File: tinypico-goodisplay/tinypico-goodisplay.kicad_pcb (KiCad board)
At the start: 2 copper layers, 42.5 x 17.8 mm, 24 parts, among them J1 AFC24-S24FIC-00, Q1 Si1308, U1 TinypicoESP32_Symbol

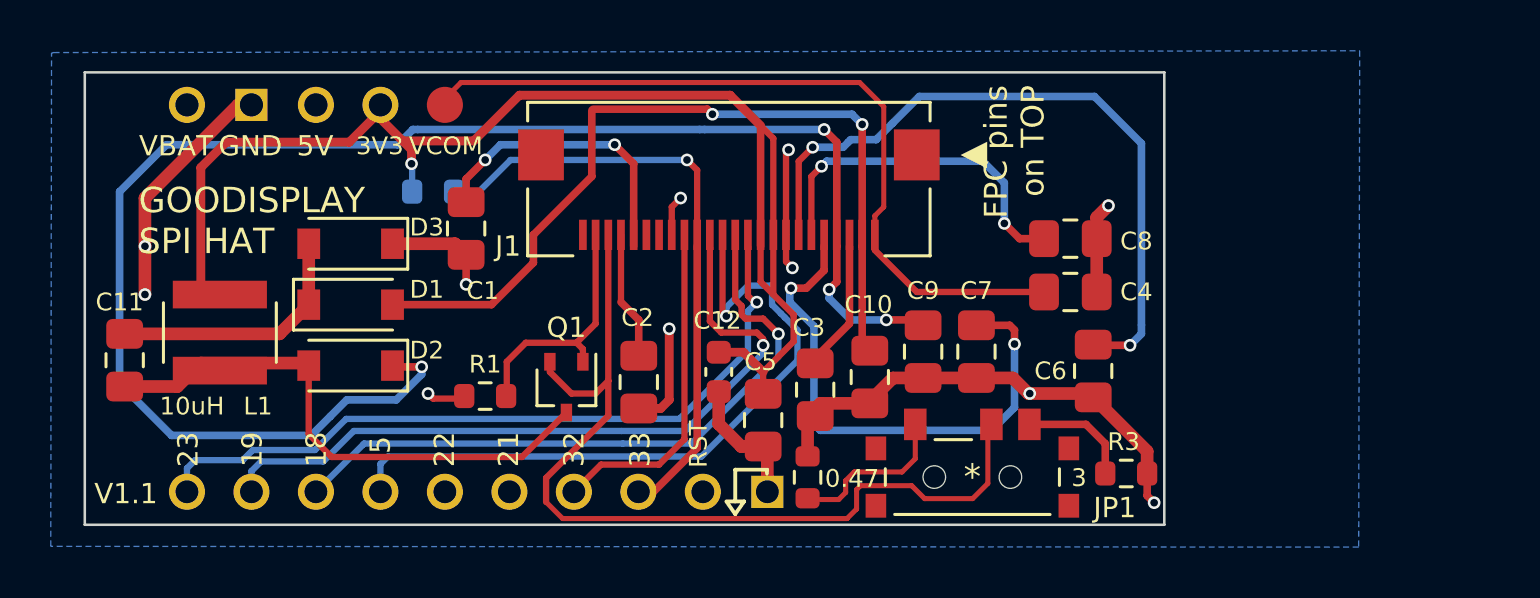
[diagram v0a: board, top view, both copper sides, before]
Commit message: #2 Add PCF8563 RTC
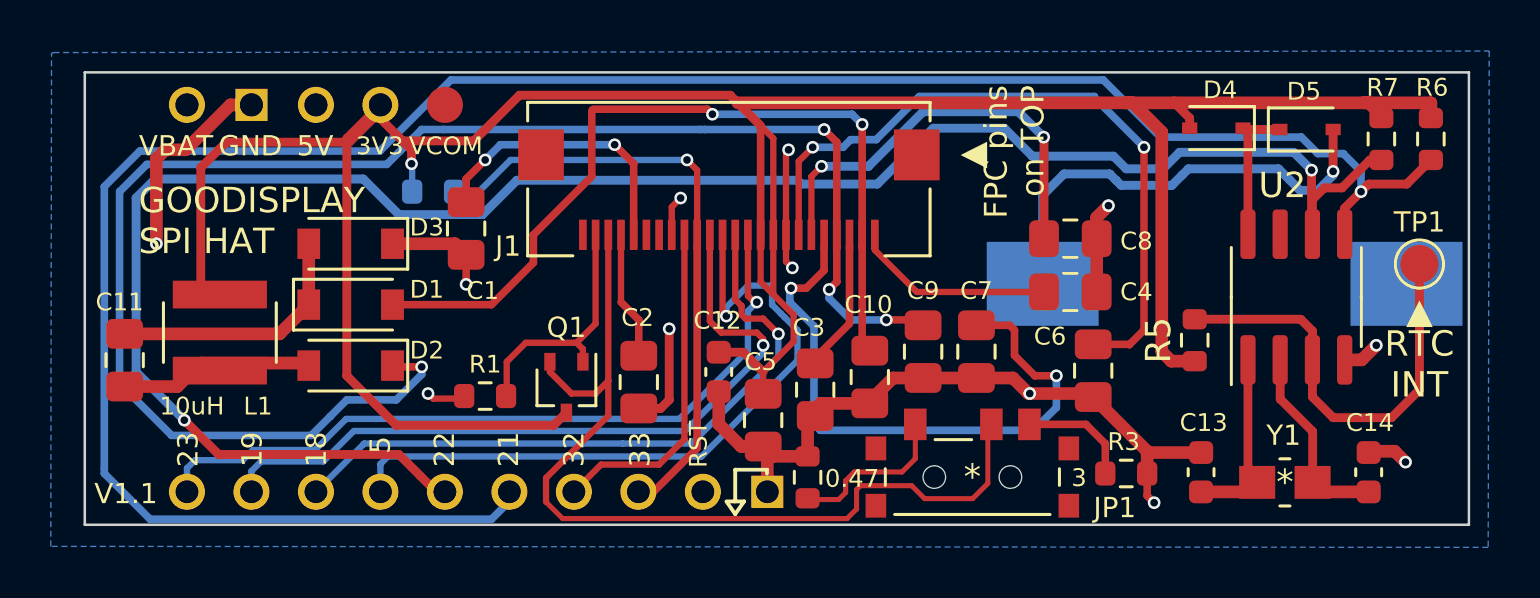
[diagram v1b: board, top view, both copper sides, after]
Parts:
- added BT1: LR44, footprint:C964716_LR44, B.Cu at (117.1, 43.0)
- added C13: 12 pF, Capacitor_SMD:C_0603_1608Metric, F.Cu at (116.2, 50.5)
- added C14: 12 pF, Capacitor_SMD:C_0603_1608Metric, F.Cu at (122.8, 50.5)
- added D4: 1N4148WS, Diode_SMD:D_SOD-323, F.Cu at (116.8, 37.0)
- added D5: 1N4148WS, Diode_SMD:D_SOD-323, F.Cu at (120.3, 37.0)
- added R5: 10 K, Resistor_SMD:R_0603_1608Metric, F.Cu at (116.0, 45.4)
- added R6: 4.7K, Resistor_SMD:R_0603_1608Metric, F.Cu at (125.2, 37.4)
- added R7: 4.7K, Resistor_SMD:R_0603_1608Metric, F.Cu at (123.3, 37.4)
- added TP1: RTC_INT, TestPoint:TestPoint_Pad_D1.5mm, F.Cu at (124.8, 42.4)
- added U2: PCF8563T, Package_SO:SOIC-8_3.9x4.9mm_P1.27mm, F.Cu at (120.0, 43.6)
- added Y1: Crystal_Small, footprint:Q13FC1350000400-Crystal, F.Cu at (119.5, 51.0)
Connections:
- Q1 pad 3: Net-(C11-Pad2) -> +3V3
- U1 pad 15: unconnected-(U1-Pad15) -> /I2C_SDA
- U1 pad 16: unconnected-(U1-Pad16) -> /I2C_SCL
- U1 pad 5: /VCOM -> unconnected-(U1-Pad5)
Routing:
- net /I2C_SDA: track 0.00 -> 87.4 mm, vias 0 -> 1
- net /I2C_SCL: track 0.00 -> 78.2 mm, vias 0 -> 2
- net +3V3: track 52.4 -> 115.3 mm
- net /VCOM: track 31.3 -> 7.95 mm
- net Net-(BT1-Pad1): track 0.00 -> 18.1 mm, vias 0 -> 1
- net Net-(R5-Pad2): track 0.00 -> 17.4 mm
- net Net-(C11-Pad2): track 21.6 -> 7.67 mm
- net Net-(C14-Pad2): track 0.00 -> 7.72 mm
- net Net-(C13-Pad2): track 0.00 -> 7.34 mm
- net Net-(D4-Pad1): track 0.00 -> 5.73 mm
- net GND: track 53.0 -> 58.7 mm, vias 11 -> 12
- net Net-(C8-Pad2): track 13.9 -> 16.9 mm
- net Net-(C7-Pad2): track 21.3 -> 24.1 mm
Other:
- board size 42.5 x 17.8 mm -> 54.5 x 17.8 mm
- board text added: "RTC INT"
- board text added: "▲"
- board text removed: "Designed by:"

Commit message: Correct routing, remove RTC TP1
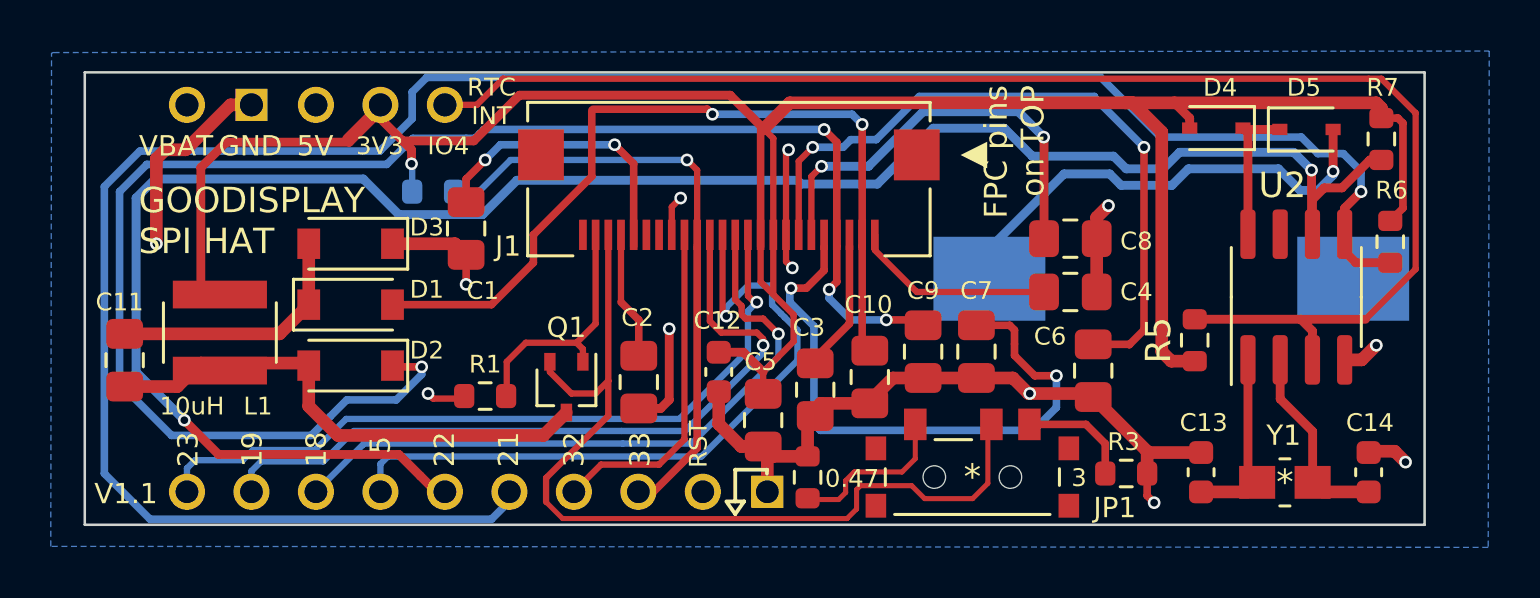
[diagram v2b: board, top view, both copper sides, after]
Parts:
- removed TP1: RTC_INT, TestPoint:TestPoint_Pad_D1.5mm
- moved R6 4.35 mm to (123.7, 41.5)
- moved BT1 2.11 mm to (115.0, 42.9)
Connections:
- Q1 pad 3: +3V3 -> Net-(C11-Pad2)
- R5 pad 2: Net-(R5-Pad2) -> /RTC_INT
- U1 pad 5: unconnected-(U1-Pad5) -> /RTC_INT
- U2 pad 3: Net-(R5-Pad2) -> /RTC_INT
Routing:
- net /RTC_INT: track 0.00 -> 56.7 mm
- net +3V3: track 115.3 -> 97.8 mm
- net Net-(R5-Pad2): track 17.4 -> 0.00 mm
- net Net-(C11-Pad2): track 7.67 -> 20.3 mm
- net Net-(BT1-Pad1): track 18.1 -> 18.8 mm
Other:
- board size 54.5 x 17.8 mm -> 52.8 x 17.8 mm
- board text added: "IO4"
- board text removed: "VCOM"
- board text removed: "▲"

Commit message: #2 Add CR1220 as optional RTC backup
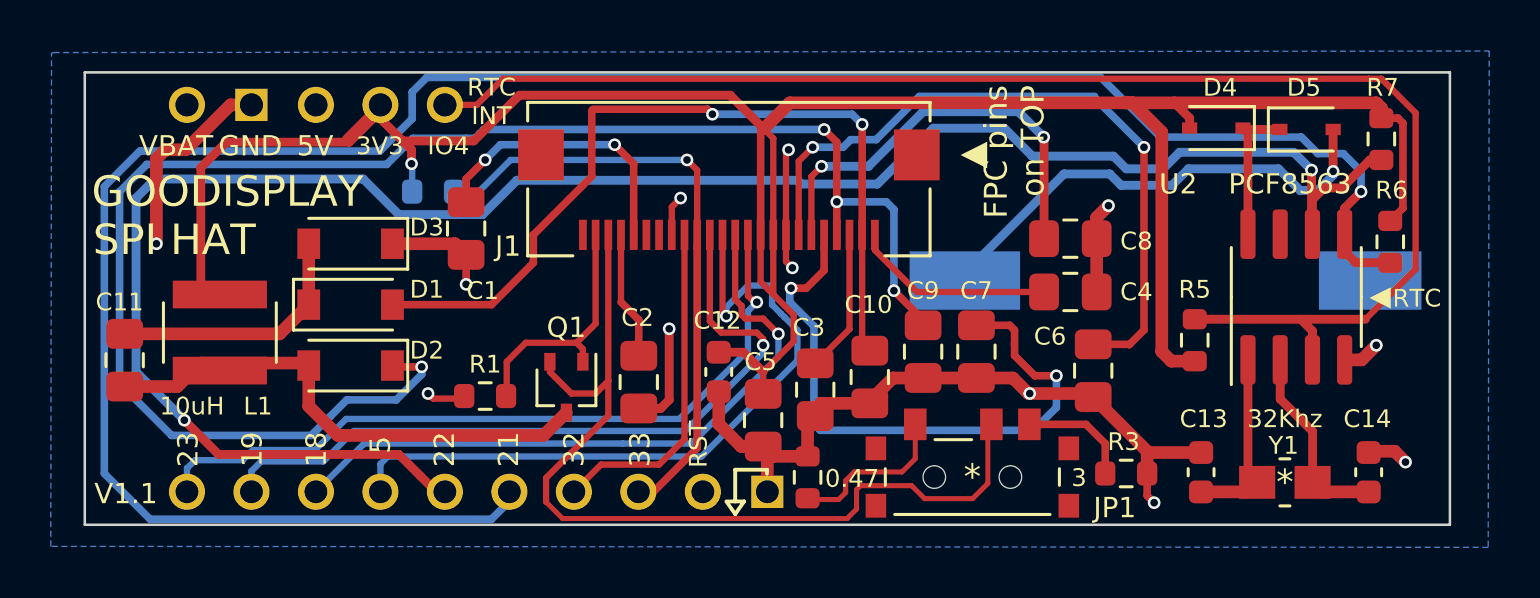
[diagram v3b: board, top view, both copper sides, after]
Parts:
- BT1: value LR44 -> CR1220; footprint footprint:C964716_LR44 -> footprint:CR12202ZX
- moved BT1 0.33 mm to (114.7, 43.0)
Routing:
- net PREVGH: track 62.7 -> 63.7 mm
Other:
- board size 52.8 x 17.8 mm -> 53.8 x 17.8 mm
- board text added: "+3V"
- board text added: "3.3V CR1220"
- board text added: "32Khz"
- board text added: "ESP32S3 tinypico ▶"
- board text added: "GOODISPLAY"
- board text added: "IO1"
- board text added: "PCF8563"
- board text added: "RTC"
- board text added: "SPI HAT"
- board text removed: "ESP32S3 tinypico IO▶"
- board text removed: "GOODISPLAY SPI HAT"

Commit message: Add latest version of GoodDisplay SPI adapter
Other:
- board text added: "+"
- board text added: "3V CR1220"
- board text removed: "+3V"
- board text removed: "3.3V CR1220"
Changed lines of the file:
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@@
     (property "Sheetfile" "File: tinypico-goodisplay.kicad_sch")
     (property "Sheetname" "")
-    (attr through_hole exclude_from_pos_files)
+    (attr through_hole exclude_from_pos_files exclude_from_bom)
     (fp_text reference "U1" (at 2.18 20.15 unlocked) (layer "F.SilkS") hide
       (effects (font (size 1 1) (thickness 0.15)))
@@
     (effects (font (size 0.9 0.9) (thickness 0.13)) (justify mirror))
   )
-  (gr_text "3.3V CR1220" (at 119.3 51.75) (layer "B.SilkS")
+  (gr_text "3V CR1220" (at 119.3 51.75) (layer "B.SilkS")
     (effects (font (size 0.8 0.8) (thickness 0.14)) (justify mirror))
   )
@@
     (effects (font (size 0.9 0.9) (thickness 0.13)) (justify mirror))
   )
-  (gr_text "+3V" (at 105.05 40 180) (layer "B.SilkS")
-    (effects (font (size 1.27 1.27) (thickness 0.254)) (justify mirror))
+  (gr_text "+" (at 103.3 43.1 180) (layer "B.SilkS")
+    (effects (font (size 2 2) (thickness 0.254)) (justify mirror))
   )
   (gr_text "ESP32S3\ntinypico ▶" (at 106.35 48.6) (layer "B.SilkS")
